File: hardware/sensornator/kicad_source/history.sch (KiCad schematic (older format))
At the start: 0 parts

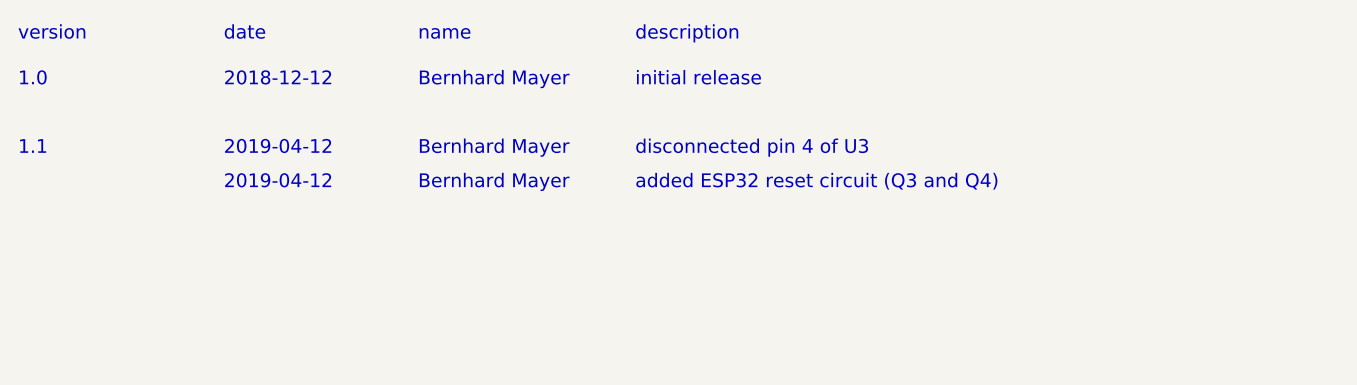
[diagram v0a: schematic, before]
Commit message: changed micro SD card socket to push pull type, updated footprint of micro USB socket
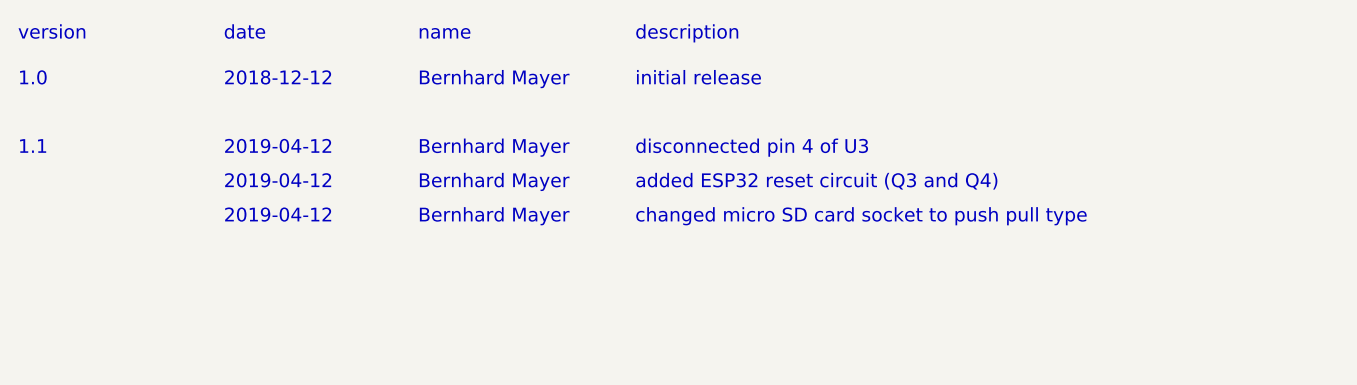
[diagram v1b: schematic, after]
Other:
- note added: "changed micro SD card socket to push pull type"
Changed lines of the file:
@@
 Text Notes 1700 1450 0    60   ~ 0
 2019-04-12
+Text Notes 3500 1600 0    60   ~ 0
+changed micro SD card socket to push pull type
+Text Notes 1700 1600 0    60   ~ 0
+2019-04-12
+Text Notes 2550 1600 0    60   ~ 0
+Bernhard Mayer
 $EndSCHEMATC

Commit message: updated schematic, added USB voltage bypass, finished layout, corrected 3D models
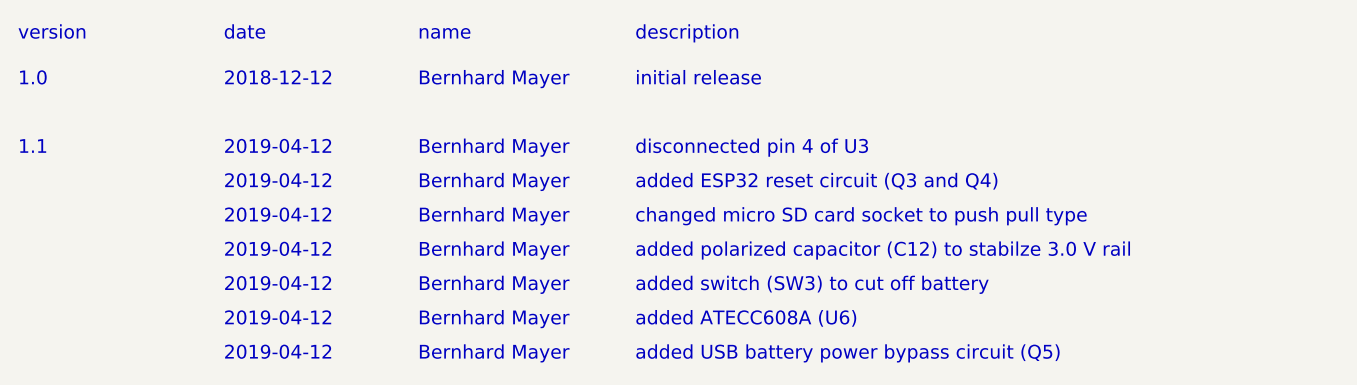
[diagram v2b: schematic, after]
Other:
- note added: "added ATECC608A (U6)"
- note added: "added USB battery power bypass circuit (Q5)"
- note added: "added polarized capacitor (C12) to stabilze 3.0 V rail"
- note added: "added switch (SW3) to cut off battery"
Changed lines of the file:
@@
 Text Notes 2550 1600 0    60   ~ 0
 Bernhard Mayer
+Text Notes 3500 1750 0    60   ~ 0
+added polarized capacitor (C12) to stabilze 3.0 V rail
+Text Notes 2550 1750 0    60   ~ 0
+Bernhard Mayer
+Text Notes 1700 1750 0    60   ~ 0
+2019-04-12
+Text Notes 3500 1900 0    60   ~ 0
+added switch (SW3) to cut off battery
+Text Notes 2550 1900 0    60   ~ 0
+Bernhard Mayer
+Text Notes 1700 1900 0    60   ~ 0
+2019-04-12
+Text Notes 3500 2050 0    60   ~ 0
+added ATECC608A (U6)
+Text Notes 2550 2050 0    60   ~ 0
+Bernhard Mayer
+Text Notes 1700 2050 0    60   ~ 0
+2019-04-12
+Text Notes 3500 2200 0    60   ~ 0
+added USB battery power bypass circuit (Q5)
+Text Notes 2550 2200 0    60   ~ 0
+Bernhard Mayer
+Text Notes 1700 2200 0    60   ~ 0
+2019-04-12
 $EndSCHEMATC
